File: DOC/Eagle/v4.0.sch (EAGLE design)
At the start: 26 parts, among them IC1 APDS-9200, IC2 PIC12LF1552, IC3 M24C01/02-XTSSOP08, M1 RF-LORA-868-SO, X1 SMA-142-0701-871/876

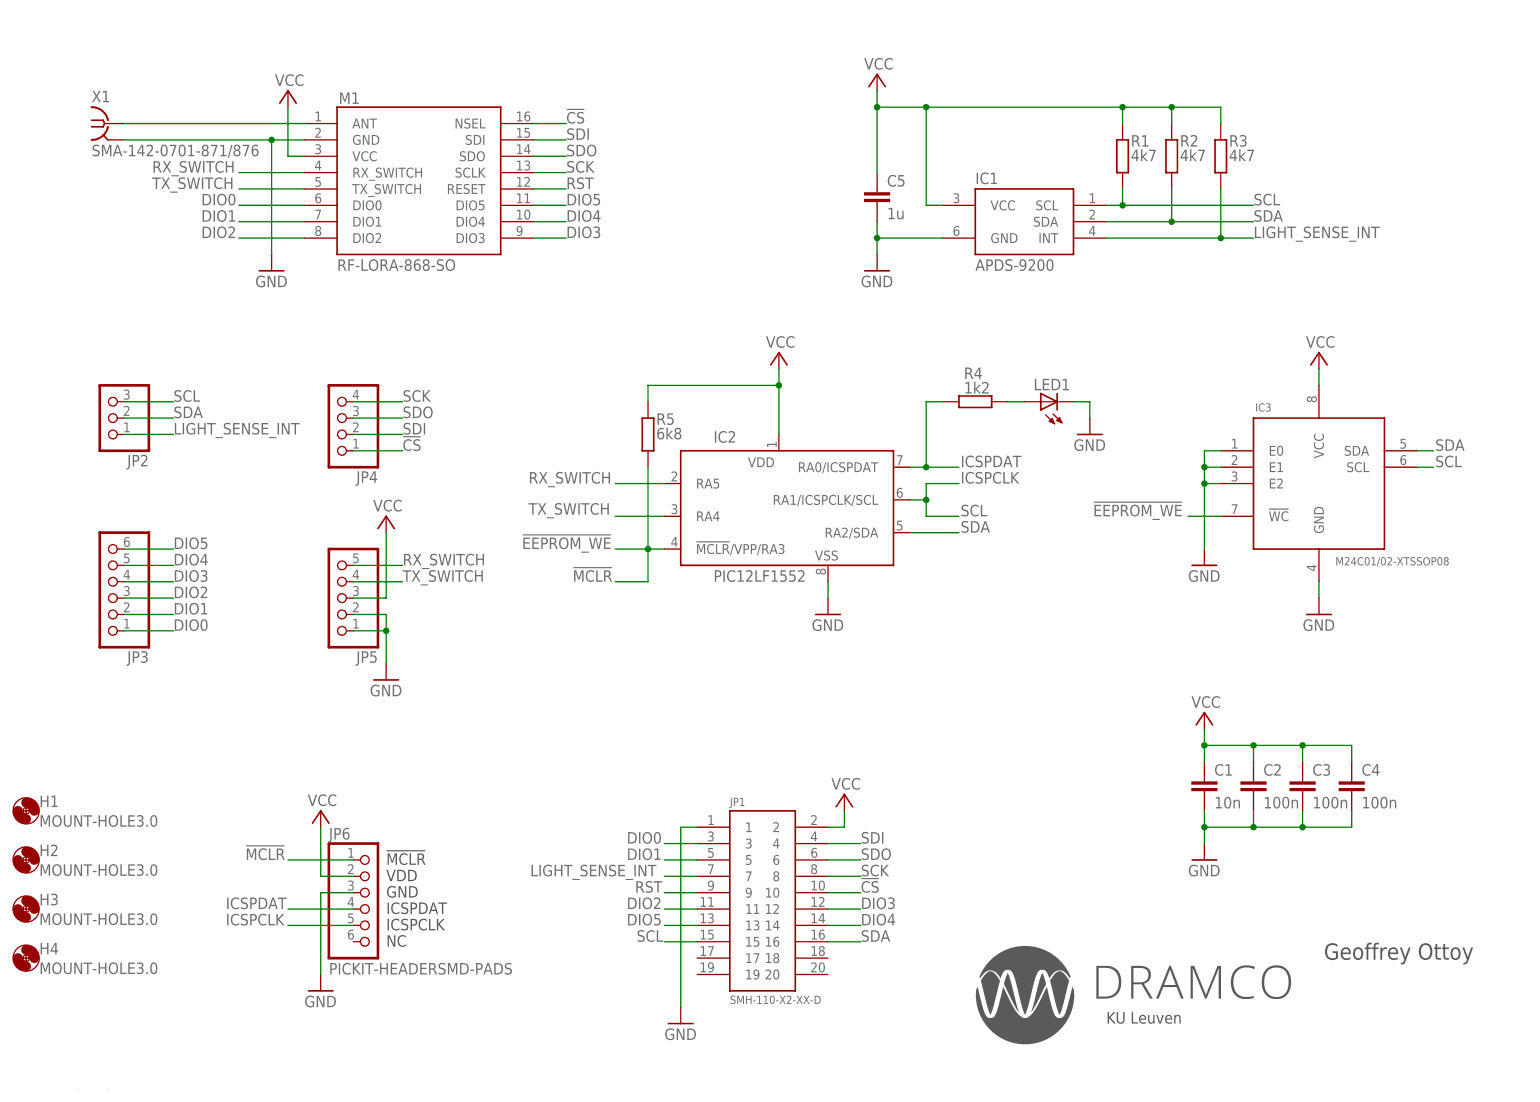
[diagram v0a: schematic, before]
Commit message: New hardware design
Added v4.0 hardware
Removed older hardware versions
v4.0 and v3.2 are the only two versions in use.
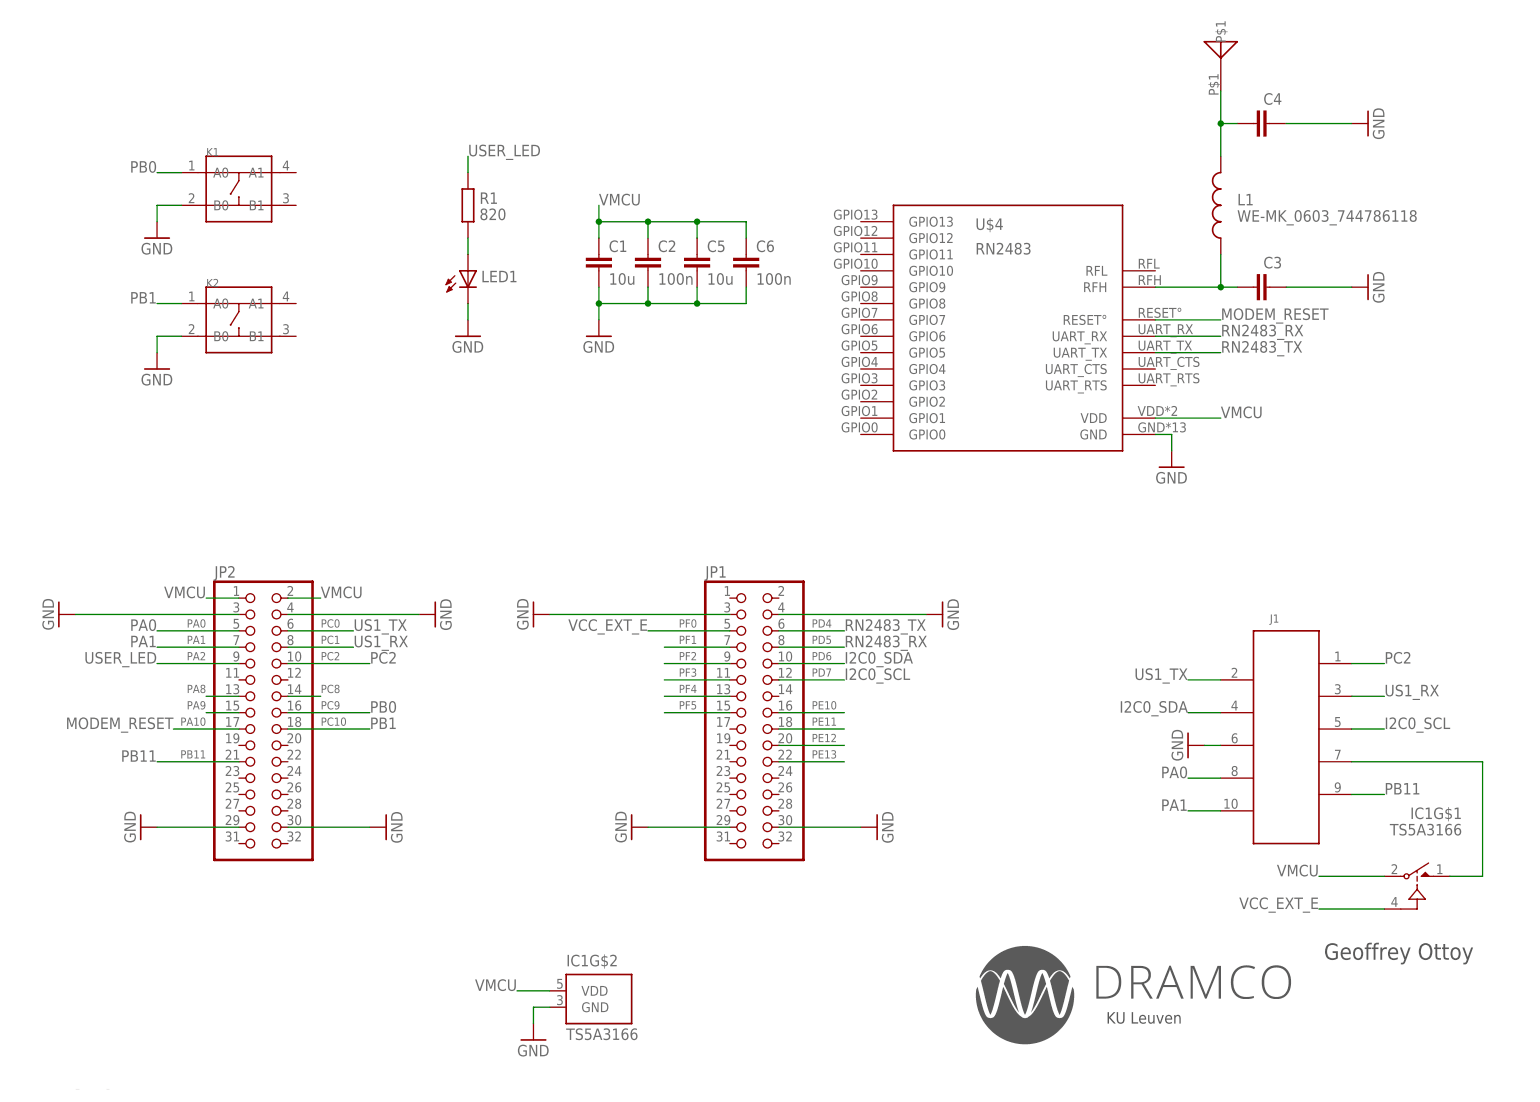
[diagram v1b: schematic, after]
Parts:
- removed H1, H2, H3, H4: MOUNT-HOLE3.0, holes:MOUNT-HOLE3.0
- removed IC2: PIC12LF1552, project:PIC12LF1552
- removed IC3: M24C01/02-XTSSOP08, project:M24C01/02-XTSSOP08
- removed JP3: (no value), pinhead:PINHD-1X6
- removed JP4: (no value), pinhead:PINHD-1X4
- removed JP5: (no value), pinhead:PINHD-1X5
- removed JP6: PICKIT-HEADERSMD-PADS, project:PICKIT-HEADERSMD-PADS
- removed M1: RF-LORA-868-SO, project:RF-LORA-868-SO
- removed R2, R3: 4k7, rcl:R-EU_M0805
- removed R4: 1k2, rcl:R-EU_M0805
- removed R5: 6k8, rcl:R-EU_M0805
- removed X1: SMA-142-0701-871/876, con-coax:SMA-142-0701-871/876
- added C6: 100n, rcl:C-EUC0805K
- added J1: (no value), project:61001018321
- added K1, K2: (no value), Seeed-Switch:SMD-SWITCH-TACTILE-SPST-NO(4P-D6.0MM)
- added L1: WE-MK_0603_744786118, project:WE-MK_0603_744786118
- added U$2: ANTENNA868, project:ANTENNA868
- added U$4: RN2483, project:RN2483
- C1: value 10n -> 10u
- C3, C4: value 100n -> (none); device rcl:C-EUC0805K -> rcl:C-EUC0603K
- C5: value 1u -> 10u
- IC1: value APDS-9200 -> TS5A3166; device project:APDS-9200 -> project:TS5A3166
- JP1: value SMH-110-X2-XX-D -> (none); device project:SMH-110-X2-XX-D -> pinhead:PINHD-2X16
- JP2: device pinhead:PINHD-1X3 -> pinhead:PINHD-2X16
- LED1: device led:LEDCHIP-LED0805 -> led:LEDCHIPLED_0805
- R1: value 4k7 -> 820; device rcl:R-EU_M0805 -> rcl:R-EU_R0805
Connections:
- removed net !CS: JP1.10, JP4.1, M1.NSEL
- removed net !MCLR: IC2.!MCLR!/VPP/RA3, IC3.!WC, JP6.1, R5.1
- removed net ANT: M1.ANT, X1.1
- removed net DIO0: JP1.3, JP3.1, M1.DIO0
- removed net DIO1: JP1.5, JP3.2, M1.DIO1
- removed net DIO2: JP1.11, JP3.3, M1.DIO2
- removed net DIO3: JP1.12, JP3.4, M1.DIO3
- removed net DIO4: JP1.14, JP3.5, M1.DIO4
- removed net DIO5: JP1.13, JP3.6, M1.DIO5
- removed net ICSPDAT: IC2.RA0/ICSPDAT, JP6.4, R4.2
- removed net LIGHT_SENSE_INT: IC1.INT, JP1.7, JP2.1, R3.1
- removed net RST: JP1.9, M1.RESET
- removed net RX_SWITCH: IC2.RA5, JP5.5, M1.RX_SWITCH
- removed net SCK: JP1.8, JP4.4, M1.SCLK
- removed net SCL: IC1.SCL, IC2.RA1/ICSPCLK/SCL, IC3.SCL, JP1.15, JP2.3, JP6.5, R1.1
- removed net SDA: IC1.SDA, IC2.RA2/SDA, IC3.SDA, JP1.16, JP2.2, R2.1
- removed net SDI: JP1.4, JP4.2, M1.SDI
- removed net SDO: JP1.6, JP4.3, M1.SDO
- removed net TX_SWITCH: IC2.RA4, JP5.4, M1.TX_SWITCH
- removed net VCC: C1.1, C2.1, C3.1, C4.1, C5.1, IC1.VCC, IC2.VDD, IC3.VCC, JP1.2, JP5.3, JP6.2, M1.VCC, R1.2, R2.2, R3.2, R5.2
- new net N$2: C3.2, L1.1, U$4.RFH
- new net N$3: C4.2, L1.2, U$2.P$1
- new net N$4: IC1G$1.NO, J1.4
- new net PA0: J1.3, JP2.5
- new net PA1: J1.1, JP2.7
- new net PA10: JP2.17, U$4.RESET°
- new net PA2: JP2.9, R1.2
- new net PA8: JP2.13
- new net PA9: JP2.15
- new net PB11: J1.2, JP2.21
- new net PC0: J1.9, JP2.6
- new net PC1: J1.8, JP2.8
- new net PC10: JP2.18, K2.A0
- new net PC2: J1.10, JP2.10
- new net PC8: JP2.14
- new net PC9: JP2.16, K1.A0
- new net PD4: JP1.6, U$4.UART_TX
- new net PD5: JP1.8, U$4.UART_RX
- new net PD6: J1.7, JP1.10
- new net PD7: J1.6, JP1.12
- new net PE10: JP1.16
- new net PE11: JP1.18
- new net PE12: JP1.20
- new net PE13: JP1.22
- new net PF0: IC1G$1.IN, JP1.5
- new net PF1: JP1.7
- new net PF2: JP1.9
- new net PF3: JP1.11
- new net PF4: JP1.13
- new net PF5: JP1.15
- new net VMCU: C1.1, C2.1, C5.1, C6.1, IC1G$1.COM, IC1G$2.VDD, JP2.1, JP2.2, U$4.VDD
- net GND: now also C3.1, C4.1, C6.2, IC1G$2.GND, J1.5, JP1.29, JP1.3, JP1.30, JP1.4, JP2.29, JP2.3, JP2.30, JP2.4, K1.B0, K2.B0, U$4.GND; no longer C3.2, C4.2, IC1.GND, IC2.VSS, IC3.E0, IC3.E1, IC3.E2, IC3.GND, JP1.1, JP5.1, JP5.2, JP6.3, M1.GND, X1.2
- net N$1: now also R1.1; no longer R4.1
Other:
- note added: "I2C0_SCL"
- note added: "I2C0_SDA"
- note added: "MODEM_RESET"
- note added: "PA0"
- note added: "PA1"
- note added: "PB0"
- note added: "PB1"
- note added: "PB11"
- note added: "PC2"
- note added: "RN2483_RX"
- note added: "RN2483_TX"
- note added: "US1_RX"
- note added: "US1_TX"
- note added: "USER_LED"
- note added: "VCC_EXT_E"
- note removed: "!EEPROM_WE"
- note removed: "ICSPCLK"
- moved on the sheet: C1, C2, C3, C4, C5, LED1, R1
